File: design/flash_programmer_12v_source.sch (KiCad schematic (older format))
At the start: 5 parts

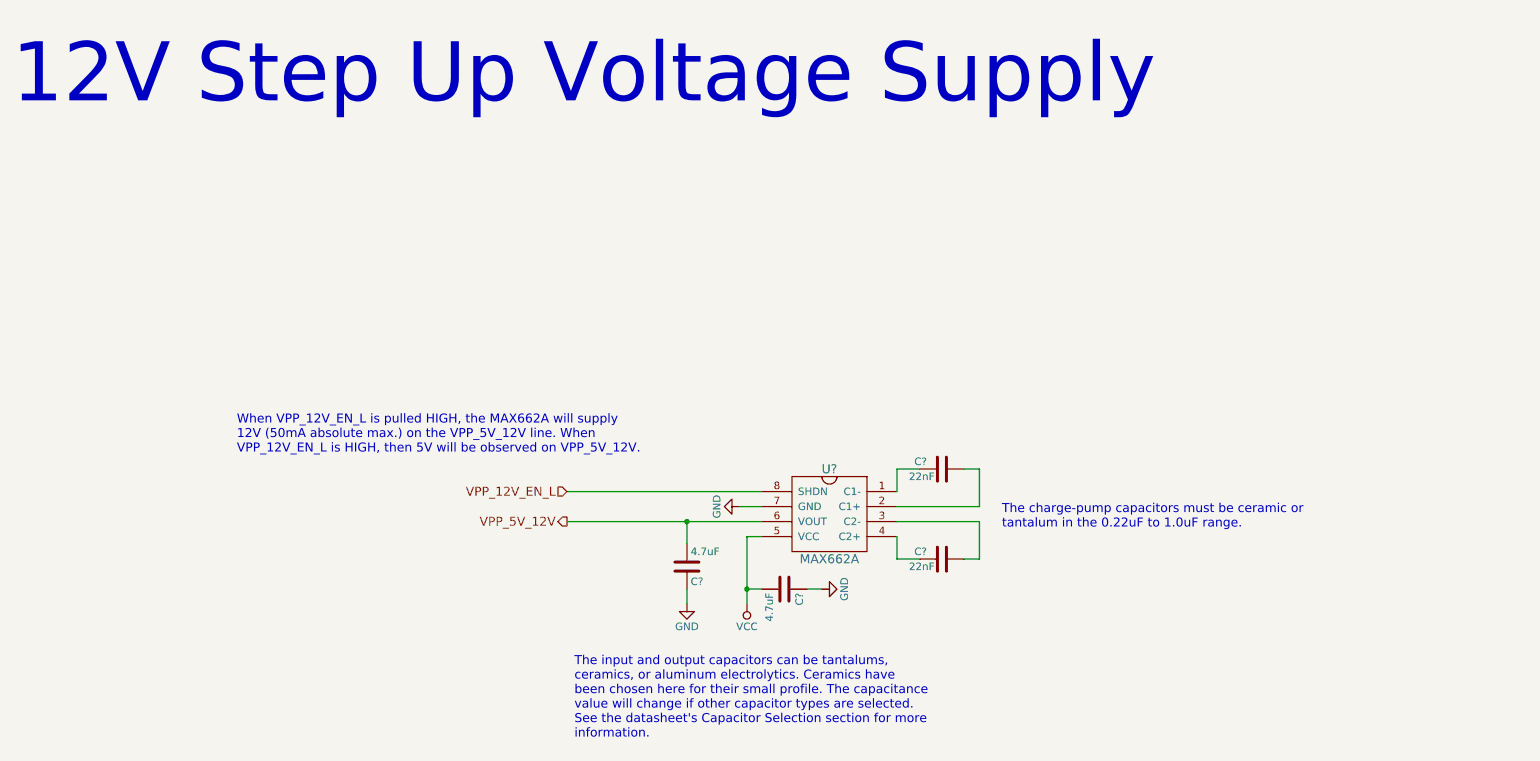
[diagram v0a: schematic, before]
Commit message: More schematic clean up
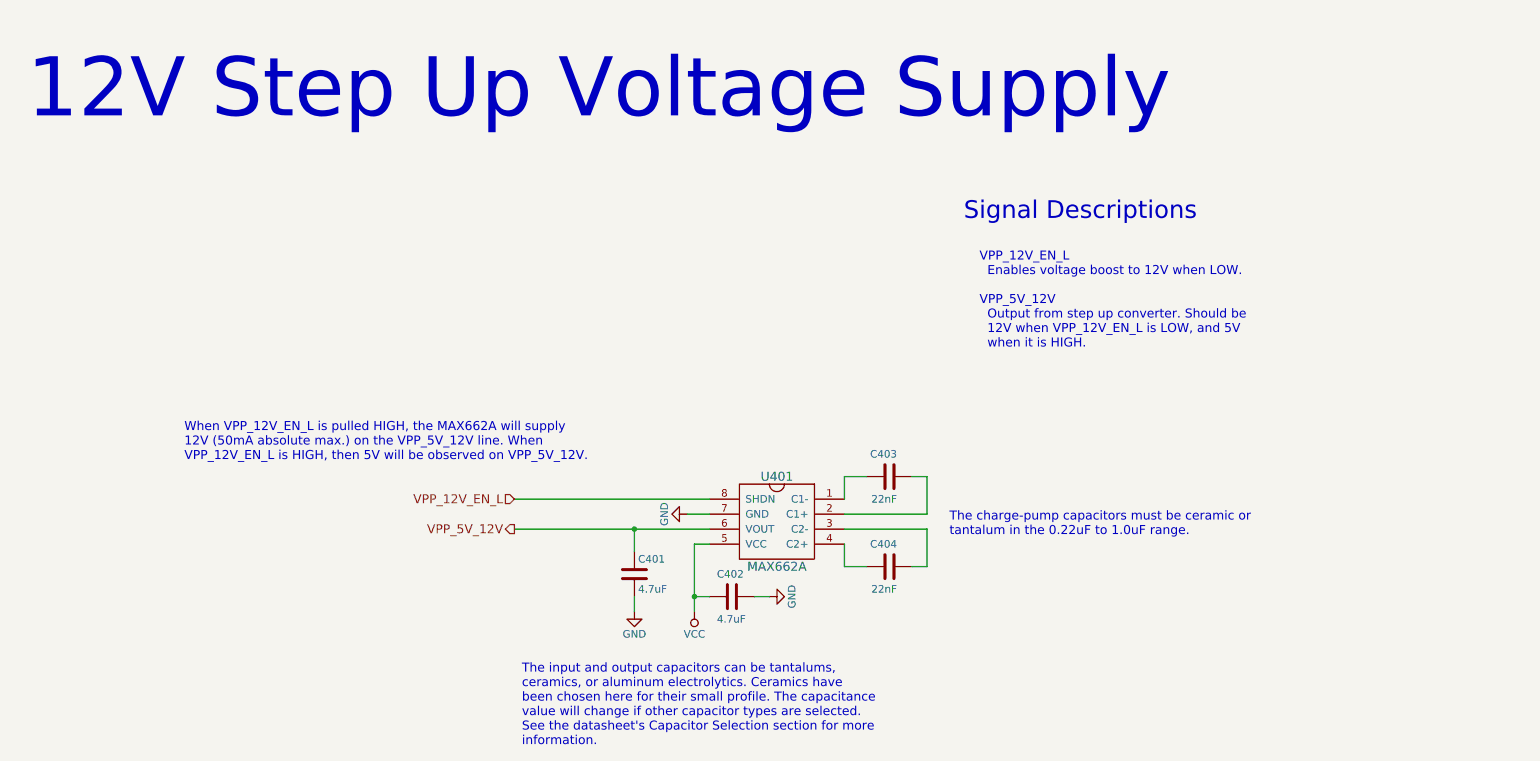
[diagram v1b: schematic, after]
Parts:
- C403, C404: renamed from C?; footprint Resistors_SMD:R_0805_HandSoldering -> Resistors_SMD:R_0603_HandSoldering
- gave numbers to parts that had none: 3
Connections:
- net GND: now also C401.2; no longer C401.1
- net VPP_5V_12V: now also C401.1; no longer C401.2
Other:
- note added: "Signal Descriptions"
- note added: "VPP_12V_EN_L\n Enables voltage boost to 12V when LOW.\n\nVPP_5V_12V\n Output from step up converter. Should be\n 12V when VPP_12V_EN_L is LOW, and 5V\n when it is HIGH."
- moved on the sheet: C401, C402, C403, C404, U401
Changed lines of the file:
@@
 EESchema Schematic File Version 2
 LIBS:gls27sf010
+LIBS:atmega328p
 LIBS:flash_programmer
 LIBS:power
@@
 EELAYER 25 0
 EELAYER END
-$Descr A4 11693 8268
+$Descr USLetter 11000 8500
 encoding utf-8
-Sheet 5 5
+Sheet 4 7
 Title "GLS27SF010 Flash Programmer"
 Date "2017-03-11"
@@
 $EndDescr
 $Comp
-L MAX662A U?
+L MAX662A U401
 U 1 1 58C44BF6
-P 6000 4000
-F 0 "U?" H 6000 4550 60  0000 C CNN
-F 1 "MAX662A" H 6000 3950 60  0000 C CNN
-F 2 "Housings_SOIC:SOIC-8_3.9x4.9mm_Pitch1.27mm" H 5900 3900 60  0001 C CNN
-F 3 "" H 5900 3900 60  0001 C CNN
-	1    6000 4000
+P 5650 4050
+F 0 "U401" H 5650 4600 60  0000 C CNN
+F 1 "MAX662A" H 5650 4000 60  0000 C CNN
+F 2 "Housings_SOIC:SOIC-8_3.9x4.9mm_Pitch1.27mm" H 5550 3950 60  0001 C CNN
+F 3 "" H 5550 3950 60  0001 C CNN
+	1    5650 4050
 	-1   0    0    -1
 $EndComp
 Wire Wire Line
-	6450 3800 7000 3800
-Wire Wire Line
-	7000 3800 7000 4050
-Wire Wire Line
-	7000 4050 6900 4050
-Wire Wire Line
-	6600 4050 6450 4050
-Wire Wire Line
-	6450 4050 6450 3900
-Wire Wire Line
-	6450 3700 7000 3700
-Wire Wire Line
-	7000 3700 7000 3450
-Wire Wire Line
-	7000 3450 6900 3450
-Wire Wire Line
-	6600 3450 6450 3450
-Wire Wire Line
-	6450 3450 6450 3600
-Wire Wire Line
-	4250 3800 5550 3800
-$Comp
-L GND #PWR?
+	6100 3850 6650 3850
+Wire Wire Line
+	6650 3850 6650 4100
+Wire Wire Line
+	6650 4100 6550 4100
+Wire Wire Line
+	6250 4100 6100 4100
+Wire Wire Line
+	6100 4100 6100 3950
+Wire Wire Line
+	6100 3750 6650 3750
+Wire Wire Line
+	6650 3750 6650 3500
+Wire Wire Line
+	6650 3500 6550 3500
+Wire Wire Line
+	6250 3500 6100 3500
+Wire Wire Line
+	6100 3500 6100 3650
+Wire Wire Line
+	3900 3850 5200 3850
+$Comp
+L GND #PWR018
 U 1 1 58C44C09
-P 5400 3700
-F 0 "#PWR?" H 5400 3450 50  0001 C CNN
-F 1 "GND" H 5400 3550 50  0000 C CNN
-F 2 "" H 5400 3700 50  0000 C CNN
-F 3 "" H 5400 3700 50  0000 C CNN
-	1    5400 3700
+P 5050 3750
+F 0 "#PWR018" H 5050 3500 50  0001 C CNN
+F 1 "GND" H 5050 3600 50  0000 C CNN
+F 2 "" H 5050 3750 50  0000 C CNN
+F 3 "" H 5050 3750 50  0000 C CNN
+	1    5050 3750
 	0    1    -1   0
 $EndComp
 $Comp
-L VCC #PWR?
+L VCC #PWR019
 U 1 1 58C44C0F
-P 5450 4350
-F 0 "#PWR?" H 5450 4200 50  0001 C CNN
-F 1 "VCC" H 5450 4500 50  0000 C CNN
-F 2 "" H 5450 4350 50  0000 C CNN
-F 3 "" H 5450 4350 50  0000 C CNN
-	1    5450 4350
+P 5100 4400
+F 0 "#PWR019" H 5100 4250 50  0001 C CNN
+F 1 "VCC" H 5100 4550 50  0000 C CNN
+F 2 "" H 5100 4400 50  0000 C CNN
+F 3 "" H 5100 4400 50  0000 C CNN
+	1    5100 4400
 	1    0    0    1
 $EndComp
-Text Notes 550  1050 0    394  ~ 0
+Text Notes 650  1150 0    394  ~ 0
 12V Step Up Voltage Supply
 $Comp
-L C C?
+L C C402
 U 1 1 58C44C16
-P 5700 4250
-F 0 "C?" H 5725 4350 50  0000 L CNN
-F 1 "4.7uF" H 5725 4150 50  0000 L CNN
-F 2 "Resistors_SMD:R_0805_HandSoldering" H 5738 4100 50  0001 C CNN
-F 3 "" H 5700 4250 50  0000 C CNN
-	1    5700 4250
+P 5350 4300
+F 0 "C402" V 5200 4200 50  0000 L CNN
+F 1 "4.7uF" V 5500 4200 50  0000 L CNN
+F 2 "Resistors_SMD:R_0805_HandSoldering" H 5388 4150 50  0001 C CNN
+F 3 "" H 5350 4300 50  0000 C CNN
+	1    5350 4300
 	0    1    1    0
 $EndComp
 $Comp
-L C C?
+L C C403
 U 1 1 58C44C25
-P 6750 3450
-F 0 "C?" V 6700 3550 50  0000 L CNN
-F 1 "22nF" V 6800 3500 50  0000 L CNN
-F 2 "Resistors_SMD:R_0805_HandSoldering" H 6788 3300 50  0001 C CNN
-F 3 "" H 6750 3450 50  0000 C CNN
-	1    6750 3450
+P 6400 3500
+F 0 "C403" V 6250 3450 50  0000 L CNN
+F 1 "22nF" V 6550 3450 50  0000 L CNN
+F 2 "Resistors_SMD:R_0603_HandSoldering" H 6438 3350 50  0001 C CNN
+F 3 "" H 6400 3500 50  0000 C CNN
+	1    6400 3500
 	0    -1   1    0
 $EndComp
 $Comp
-L C C?
+L C C404
 U 1 1 58C44C2C
-P 6750 4050
-F 0 "C?" V 6700 4150 50  0000 L CNN
-F 1 "22nF" V 6800 4100 50  0000 L CNN
-F 2 "Resistors_SMD:R_0805_HandSoldering" H 6788 3900 50  0001 C CNN
-F 3 "" H 6750 4050 50  0000 C CNN
-	1    6750 4050
+P 6400 4100
+F 0 "C404" V 6250 4050 50  0000 L CNN
+F 1 "22nF" V 6550 4050 50  0000 L CNN
+F 2 "Resistors_SMD:R_0603_HandSoldering" H 6438 3950 50  0001 C CNN
+F 3 "" H 6400 4100 50  0000 C CNN
+	1    6400 4100
 	0    -1   1    0
 $EndComp
 Wire Wire Line
-	5550 3900 5450 3900
-Wire Wire Line
-	5450 3900 5450 4350
-$Comp
-L C C?
+	5200 3950 5100 3950
+Wire Wire Line
+	5100 3950 5100 4400
+$Comp
+L C C401
 U 1 1 58C44C35
-P 5050 4100
-F 0 "C?" H 5075 4200 50  0000 L CNN
-F 1 "4.7uF" H 5075 4000 50  0000 L CNN
-F 2 "Resistors_SMD:R_0805_HandSoldering" H 5088 3950 50  0001 C CNN
-F 3 "" H 5050 4100 50  0000 C CNN
-	1    5050 4100
-	1    0    0    1
-$EndComp
-Wire Wire Line
-	4250 3600 5550 3600
-Wire Wire Line
-	5050 3950 5050 3800
-Connection ~ 5050 3800
-Wire Wire Line
-	5050 4250 5050 4350
-$Comp
-L GND #PWR?
+P 4700 4150
+F 0 "C401" H 4725 4250 50  0000 L CNN
+F 1 "4.7uF" H 4725 4050 50  0000 L CNN
+F 2 "Resistors_SMD:R_0805_HandSoldering" H 4738 4000 50  0001 C CNN
+F 3 "" H 4700 4150 50  0000 C CNN
+	1    4700 4150
+	1    0    0    -1
+$EndComp
+Wire Wire Line
+	3900 3650 5200 3650
+Wire Wire Line
+	4700 4000 4700 3850
+Connection ~ 4700 3850
+Wire Wire Line
+	4700 4300 4700 4400
+$Comp
+L GND #PWR020
 U 1 1 58C44C40
-P 5050 4350
-F 0 "#PWR?" H 5050 4100 50  0001 C CNN
-F 1 "GND" H 5050 4200 50  0000 C CNN
-F 2 "" H 5050 4350 50  0000 C CNN
-F 3 "" H 5050 4350 50  0000 C CNN
-	1    5050 4350
+P 4700 4400
+F 0 "#PWR020" H 4700 4150 50  0001 C CNN
+F 1 "GND" H 4700 4250 50  0000 C CNN
+F 2 "" H 4700 4400 50  0000 C CNN
+F 3 "" H 4700 4400 50  0000 C CNN
+	1    4700 4400
 	-1   0    0    -1
 $EndComp
-Text HLabel 4250 3600 0    60   Input ~ 0
+Text HLabel 3900 3650 0    60   Input ~ 0
 VPP_12V_EN_L
 $Comp
-L GND #PWR?
+L GND #PWR021
 U 1 1 58C44C4A
-P 5950 4250
-F 0 "#PWR?" H 5950 4000 50  0001 C CNN
-F 1 "GND" H 5950 4100 50  0000 C CNN
-F 2 "" H 5950 4250 50  0000 C CNN
-F 3 "" H 5950 4250 50  0000 C CNN
-	1    5950 4250
+P 5600 4300
+F 0 "#PWR021" H 5600 4050 50  0001 C CNN
+F 1 "GND" H 5600 4150 50  0000 C CNN
+F 2 "" H 5600 4300 50  0000 C CNN
+F 3 "" H 5600 4300 50  0000 C CNN
+	1    5600 4300
 	0    -1   -1   0
 $EndComp
 Wire Wire Line
-	5400 3700 5550 3700
-Text HLabel 4250 3800 0    60   Output ~ 0
+	5050 3750 5200 3750
+Text HLabel 3900 3850 0    60   Output ~ 0
 VPP_5V_12V
-Text Notes 2050 3350 0    60   ~ 0
+Text Notes 1700 3400 0    60   ~ 0
 When VPP_12V_EN_L is pulled HIGH, the MAX662A will supply \n12V (50mA absolute max.) on the VPP_5V_12V line. When \nVPP_12V_EN_L is HIGH, then 5V will be observed on VPP_5V_12V.
-Text Notes 7150 3850 0    60   ~ 0
+Text Notes 6800 3900 0    60   ~ 0
 The charge-pump capacitors must be ceramic or\ntantalum in the 0.22uF to 1.0uF range.
 Wire Wire Line
-	5550 4250 5450 4250
-Connection ~ 5450 4250
-Wire Wire Line
-	5850 4250 5950 4250
-Text Notes 4300 5250 0    60   ~ 0
+	5200 4300 5100 4300
+Connection ~ 5100 4300
+Wire Wire Line
+	5500 4300 5600 4300
+Text Notes 3950 5300 0    60   ~ 0
 The input and output capacitors can be tantalums,\nceramics, or aluminum electrolytics. Ceramics have\nbeen chosen here for their small profile. The capacitance\nvalue will change if other capacitor types are selected.\nSee the datasheet's Capacitor Selection section for more \ninformation.
+Text Notes 8450 1800 2    118  ~ 0
+Signal Descriptions
+Text Notes 7000 2650 0    60   ~ 0
+VPP_12V_EN_L\n  Enables voltage boost to 12V when LOW.\n\nVPP_5V_12V\n  Output from step up converter. Should be\n  12V when VPP_12V_EN_L is LOW, and 5V\n  when it is HIGH.
 $EndSCHEMATC
